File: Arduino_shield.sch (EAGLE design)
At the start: 7 parts, among them X1 6PIN_CON

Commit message: Schematics_v1
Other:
- note added: "Srylab 03/2022 Arduino Shield v1.0 Jacopo De Santis"
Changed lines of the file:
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@@
 <sheet>
 <plain>
+<text x="106.68" y="-35.56" size="2.54" layer="91" font="vector">Srylab 03/2022
+Arduino Shield v1.0
+Jacopo De Santis</text>
 </plain>
 <instances>
@@
 </schematic>
 </drawing>
+<compatibility>
+<note version="6.3" minversion="6.2.2" severity="warning">
+Since Version 6.2.2 text objects can contain more than one line,
+which will not be processed correctly with this version.
+</note>
+</compatibility>
 </eagle>

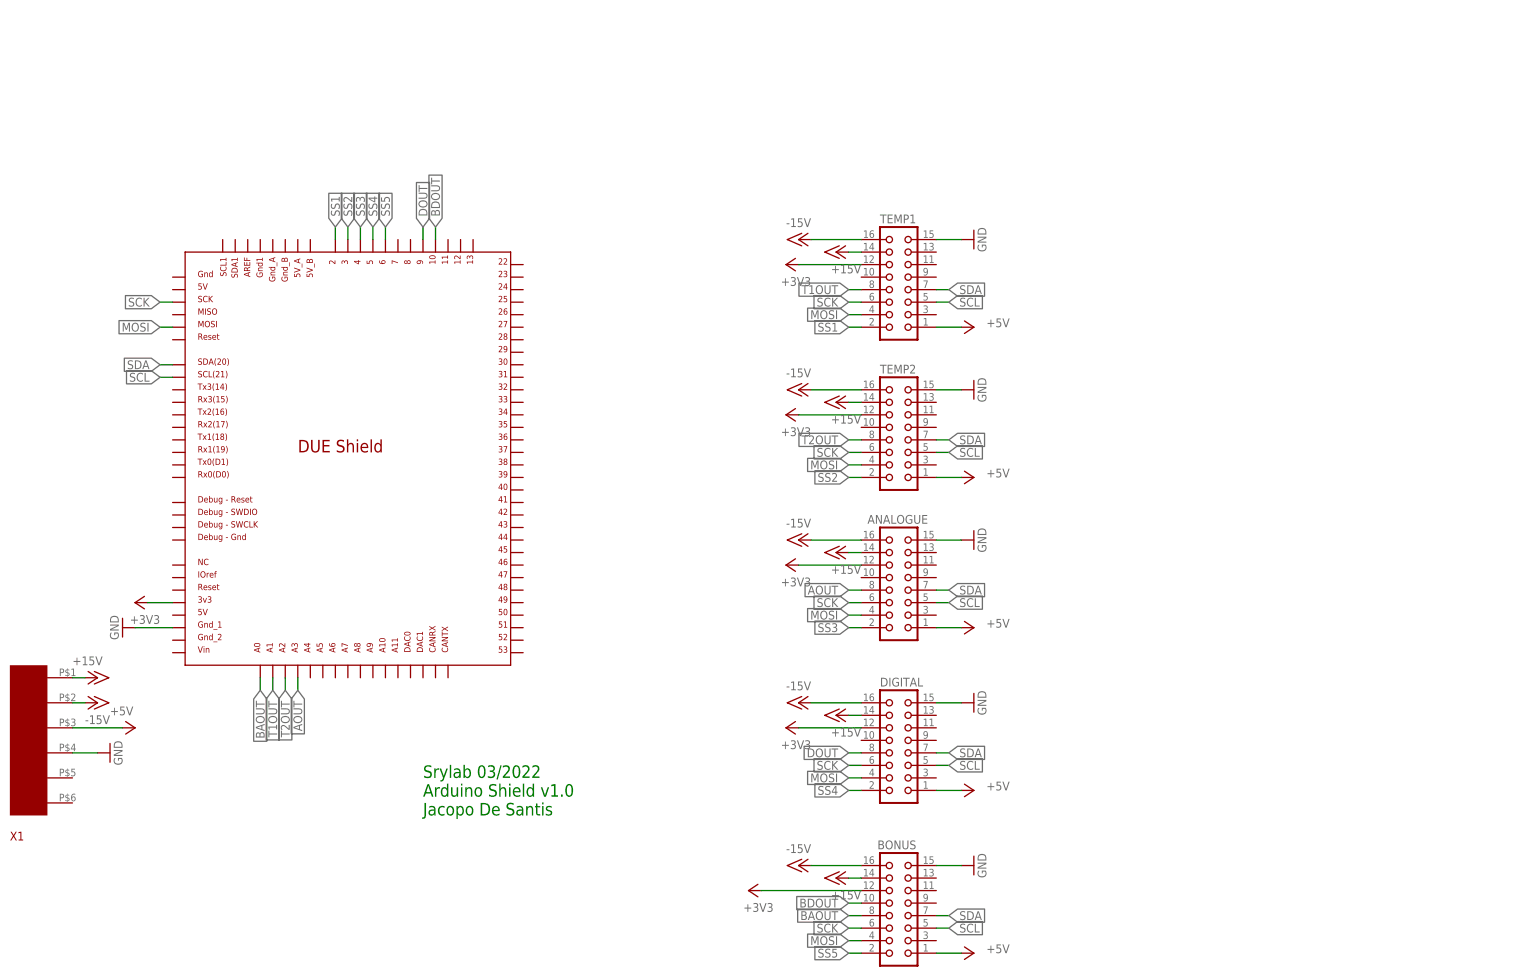
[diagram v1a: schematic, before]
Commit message: Official_flat_cable_connections
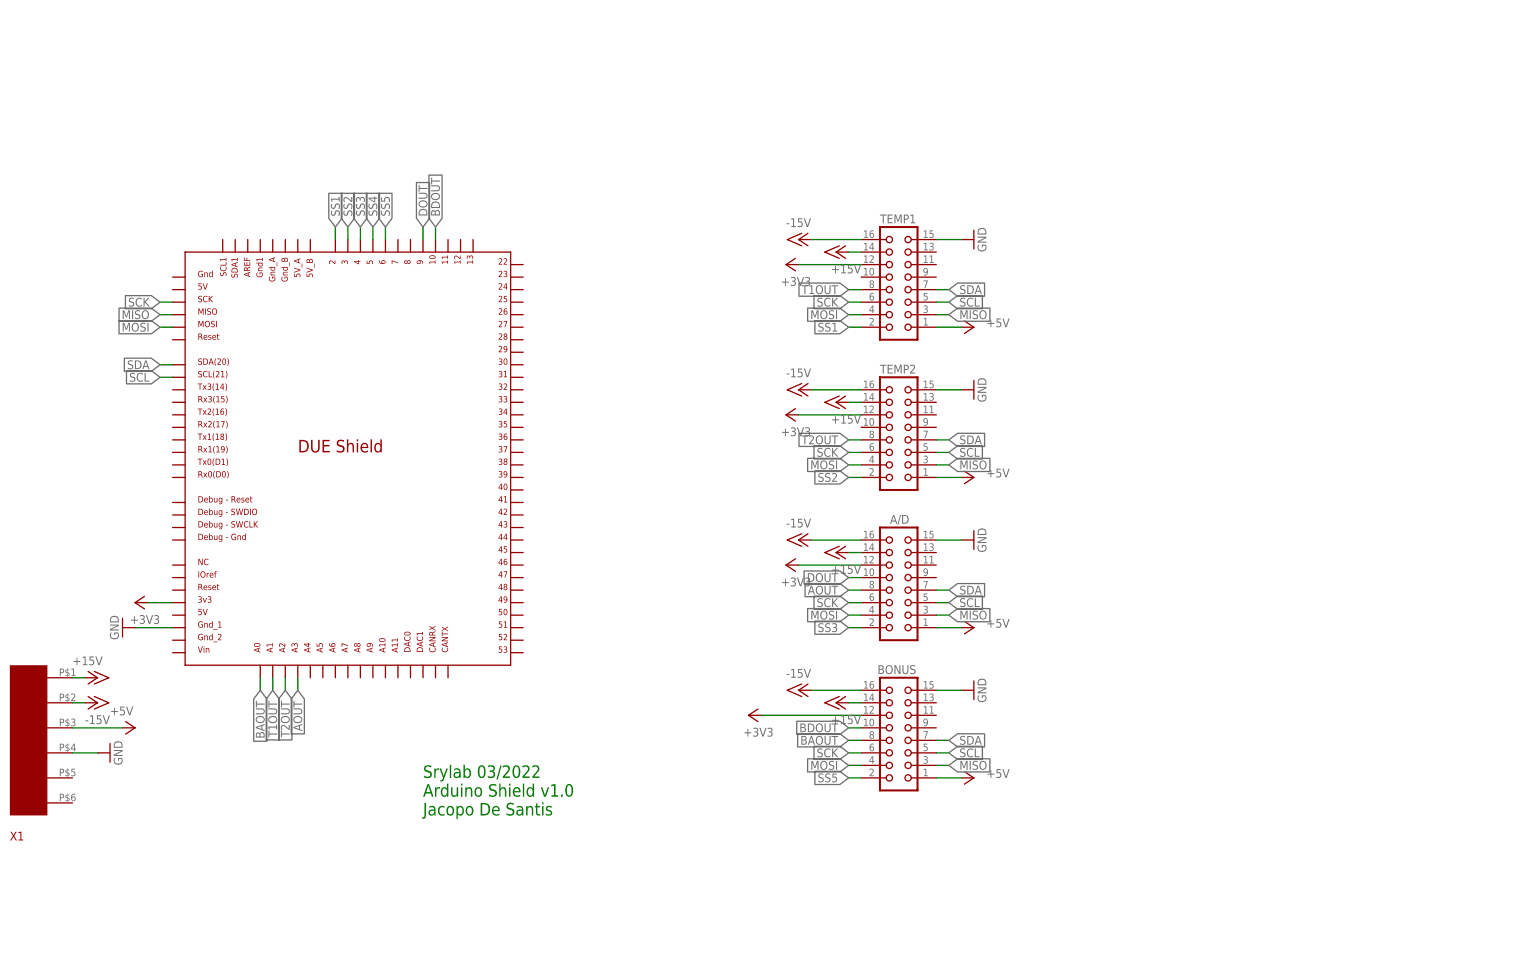
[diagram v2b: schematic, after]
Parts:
- removed DIGITAL: (no value), con-harting:CON16L
- renumbered ANALOGUE to A/D
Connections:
- new net MISO: A/D.3, BONUS.3, TEMP1.3, TEMP2.3, U$1.MISO_ICSP
- net +15V: no longer DIGITAL.14
- net +3V3: no longer DIGITAL.12
- net +5V: no longer DIGITAL.1
- net -15V: no longer DIGITAL.16
- net DOUT: now also A/D.10; no longer DIGITAL.8
- net GND: no longer DIGITAL.15
- net MOSI: no longer DIGITAL.4
- net SCK: no longer DIGITAL.6
- net SCL: no longer DIGITAL.5
- net SDA: no longer DIGITAL.7
- net SS4: no longer DIGITAL.2
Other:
- moved on the sheet: BONUS

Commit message: Added_relays
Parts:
- added DEV1, DEV2, DEV3, DEV4, DEV5, DEV6, DEV7, DEV8: SMA-F_A0201, 1AKarstenLib:SMA-F_A0201
- added REL1, REL2, REL3, REL4: TE_2-1462039-6TE_2-1462039-6_0_0, TE - 2-1462039-6:TE_2-1462039-6TE_2-1462039-6_0_0
- renumbered X1 to PWR
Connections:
- new net D1A: DEV1.1, REL2.6
- new net D1B: DEV1.2, REL2.7
- new net D2A: DEV2.1, REL2.3
- new net D2B: DEV2.2, REL2.2
- new net D3A: DEV3.1
- new net D3B: DEV3.2
- new net D4A: DEV4.1, REL1.6
- new net D4B: DEV4.2, REL1.7
- new net D5A: DEV5.1, REL1.3, REL4.6
- new net D5B: DEV5.2, REL1.2, REL4.7
- new net D6A: DEV6.1, REL4.3
- new net D6B: DEV6.2, REL4.2
- new net D7A: DEV7.1, REL3.6
- new net D7B: DEV7.2, REL3.7
- new net D8A: DEV8.1, REL3.3
- new net D8B: DEV8.2, REL3.2
- new net RR1: REL1.1, U$1.10
- new net RR2: REL2.1, U$1.11
- new net RR3: REL3.1, U$1.12
- new net RR4: REL4.1, U$1.13
- net BDOUT: now also U$1.9; no longer U$1.10
- net DOUT: now also U$1.8; no longer U$1.9
- net GND: now also REL1.8, REL2.8, REL3.8, REL4.8

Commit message: Final_v1
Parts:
- added BUZZER: 3PIN_CON, CoilCircuitLibrary_E7:3PIN_CON
- added EXTRAANALOGUE, EXTRADIG: (no value), pinhead:PINHD-2X16
- DEV1, DEV2, DEV3, DEV4, DEV5, DEV6, DEV7, DEV8: value SMA-F_A0201 -> 3PIN_CON; device 1AKarstenLib:SMA-F_A0201 -> CoilCircuitLibrary_E7:3PIN_CON
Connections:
- new net BUZZ: BUZZER.P$2, U$1.7
- new net D22: EXTRADIG.1, U$1.22
- new net D23: EXTRADIG.2, U$1.23
- new net D24: EXTRADIG.3, U$1.24
- new net D25: EXTRADIG.4, U$1.25
- new net D26: EXTRADIG.5, U$1.26
- new net D27: EXTRADIG.6, U$1.27
- new net D28: EXTRADIG.7, U$1.28
- new net D29: EXTRADIG.8, U$1.29
- new net D30: EXTRADIG.9, U$1.30
- new net D31: EXTRADIG.10, U$1.31
- new net D32: EXTRADIG.11, U$1.32
- new net D33: EXTRADIG.12, U$1.33
- new net D34: EXTRADIG.13, U$1.34
- new net D35: EXTRADIG.14, U$1.35
- new net D36: EXTRADIG.15, U$1.36
- new net D37: EXTRADIG.16, U$1.37
- new net D38: EXTRADIG.17, U$1.38
- new net D39: EXTRADIG.18, U$1.39
- new net D40: EXTRADIG.19, U$1.40
- new net D41: EXTRADIG.20, U$1.41
- new net D42: EXTRADIG.21, U$1.42
- new net D43: EXTRADIG.22, U$1.43
- new net D44: EXTRADIG.23, U$1.44
- new net D45: EXTRADIG.24, U$1.45
- new net D46: EXTRADIG.25, U$1.46
- new net D47: EXTRADIG.26, U$1.47
- new net D48: EXTRADIG.27, U$1.48
- new net D49: EXTRADIG.28, U$1.49
- new net D50: EXTRADIG.29, U$1.50
- new net D51: EXTRADIG.30, U$1.51
- new net D52: EXTRADIG.31, U$1.52
- new net D53: EXTRADIG.32, U$1.53
- new net N$57: EXTRAANALOGUE.2, U$1.A4
- new net N$58: EXTRAANALOGUE.4, U$1.A5
- new net N$59: EXTRAANALOGUE.6, U$1.A6
- new net N$60: EXTRAANALOGUE.8, U$1.A7
- new net N$61: EXTRAANALOGUE.10, U$1.A8
- new net N$62: EXTRAANALOGUE.12, U$1.A9
- new net N$63: EXTRAANALOGUE.14, U$1.A10
- new net N$64: EXTRAANALOGUE.16, U$1.A11
- net +15V: now also EXTRAANALOGUE.1
- net +3V3: now also EXTRAANALOGUE.7
- net +5V: now also EXTRAANALOGUE.5
- net -15V: now also EXTRAANALOGUE.3
- net D1A: now also DEV1.P$3; no longer DEV1.1
- net D1B: now also DEV1.P$2; no longer DEV1.2
- net D2A: now also DEV2.P$3; no longer DEV2.1
- net D2B: now also DEV2.P$2; no longer DEV2.2
- net D3A: now also DEV3.P$3, REL1.6; no longer DEV3.1
- net D3B: now also DEV3.P$2, REL1.7; no longer DEV3.2
- net D4A: now also DEV4.P$3, REL1.3; no longer DEV4.1, REL1.6
- net D4B: now also DEV4.P$2, REL1.2; no longer DEV4.2, REL1.7
- net D5A: now also DEV5.P$3; no longer DEV5.1, REL1.3
- net D5B: now also DEV5.P$2; no longer DEV5.2, REL1.2
- net D6A: now also DEV6.P$3; no longer DEV6.1
- net D6B: now also DEV6.P$2; no longer DEV6.2
- net D7A: now also DEV7.P$3; no longer DEV7.1
- net D7B: now also DEV7.P$2; no longer DEV7.2
- net D8A: now also DEV8.P$3; no longer DEV8.1
- net D8B: now also DEV8.P$2; no longer DEV8.2
- net GND: now also BUZZER.P$3, EXTRAANALOGUE.9

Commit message: Initial_handmade_routing
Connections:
- removed net SS5: BONUS.2, U$1.6
- net D1A: now also DEV1.P$2, REL1.6; no longer DEV1.P$3, REL2.6
- net D1B: now also DEV1.P$3, REL1.7; no longer DEV1.P$2, REL2.7
- net D22: now also EXTRADIG.2; no longer EXTRADIG.1
- net D23: now also EXTRADIG.1; no longer EXTRADIG.2
- net D24: now also EXTRADIG.4; no longer EXTRADIG.3
- net D25: now also EXTRADIG.3; no longer EXTRADIG.4
- net D26: now also EXTRADIG.6; no longer EXTRADIG.5
- net D27: now also EXTRADIG.5; no longer EXTRADIG.6
- net D28: now also EXTRADIG.8; no longer EXTRADIG.7
- net D29: now also EXTRADIG.7; no longer EXTRADIG.8
- net D2A: now also DEV2.P$2, REL1.3; no longer DEV2.P$3, REL2.3
- net D2B: now also DEV2.P$3, REL1.2; no longer DEV2.P$2, REL2.2
- net D30: now also EXTRADIG.10; no longer EXTRADIG.9
- net D31: now also EXTRADIG.9; no longer EXTRADIG.10
- net D32: now also EXTRADIG.12; no longer EXTRADIG.11
- net D33: now also EXTRADIG.11; no longer EXTRADIG.12
- net D34: now also EXTRADIG.14; no longer EXTRADIG.13
- net D35: now also EXTRADIG.13; no longer EXTRADIG.14
- net D36: now also EXTRADIG.16; no longer EXTRADIG.15
- net D37: now also EXTRADIG.15; no longer EXTRADIG.16
- net D38: now also EXTRADIG.18; no longer EXTRADIG.17
- net D39: now also EXTRADIG.17; no longer EXTRADIG.18
- net D3A: now also DEV3.P$2, REL2.6; no longer DEV3.P$3, REL1.6
- net D3B: now also DEV3.P$3, REL2.7; no longer DEV3.P$2, REL1.7
- net D40: now also EXTRADIG.20; no longer EXTRADIG.19
- net D41: now also EXTRADIG.19; no longer EXTRADIG.20
- net D42: now also EXTRADIG.22; no longer EXTRADIG.21
- net D43: now also EXTRADIG.21; no longer EXTRADIG.22
- net D44: now also EXTRADIG.24; no longer EXTRADIG.23
- net D45: now also EXTRADIG.23; no longer EXTRADIG.24
- net D46: now also EXTRADIG.26; no longer EXTRADIG.25
- net D47: now also EXTRADIG.25; no longer EXTRADIG.26
- net D48: now also EXTRADIG.28; no longer EXTRADIG.27
- net D49: now also EXTRADIG.27; no longer EXTRADIG.28
- net D4A: now also DEV4.P$2, REL2.3; no longer DEV4.P$3, REL1.3
- net D4B: now also DEV4.P$3, REL2.2; no longer DEV4.P$2, REL1.2
- net D50: now also EXTRADIG.30; no longer EXTRADIG.29
- net D51: now also EXTRADIG.29; no longer EXTRADIG.30
- net D52: now also EXTRADIG.32; no longer EXTRADIG.31
- net D53: now also EXTRADIG.31; no longer EXTRADIG.32
- net D5A: now also DEV5.P$2, REL3.6; no longer DEV5.P$3, REL4.6
- net D5B: now also DEV5.P$3, REL3.7; no longer DEV5.P$2, REL4.7
- net D6A: now also DEV6.P$2, REL3.3; no longer DEV6.P$3, REL4.3
- net D6B: now also DEV6.P$3, REL3.2; no longer DEV6.P$2, REL4.2
- net D7A: now also DEV7.P$2, REL4.6; no longer DEV7.P$3, REL3.6
- net D7B: now also DEV7.P$3, REL4.7; no longer DEV7.P$2, REL3.7
- net D8A: now also DEV8.P$2, REL4.3; no longer DEV8.P$3, REL3.3
- net D8B: now also DEV8.P$3, REL4.2; no longer DEV8.P$2, REL3.2
- net GND: now also U$1.5V_ICSP, U$1.GND1, U$1.GND_2, U$1.GND_A, U$1.GND_B
- net RR1: now also REL2.1; no longer REL1.1
- net RR2: now also REL1.1; no longer REL2.1
- net RR3: now also REL4.1; no longer REL3.1
- net RR4: now also REL3.1; no longer REL4.1
- net SS4: now also BONUS.2
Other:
- moved on the sheet: REL1, REL2, REL3, REL4
